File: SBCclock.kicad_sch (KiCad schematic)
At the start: 18 parts, among them J1 clocks, J2 quadrature, J3 power, U1 74HCT14, U2 74HCT163, U3 74HCT112, U4 74ACT07, U5 74HCT153, Y2 GTXO-S14V

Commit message: revised board - tested
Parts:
- added D3: RED, LED_SMD:LED_0805_2012Metric_Pad1.15x1.40mm_HandSolder, symbol Device:LED
- added D4: YELLOW, LED_SMD:LED_0805_2012Metric_Pad1.15x1.40mm_HandSolder, symbol Device:LED
- added D5: GREEN, LED_SMD:LED_0805_2012Metric_Pad1.15x1.40mm_HandSolder, symbol Device:LED
- added R2, R8, R9: 330R, Resistor_SMD:R_0805_2012Metric_Pad1.20x1.40mm_HandSolder, symbol Device:R
- added SW1: SW_Push, Button_Switch_SMD:SW_SPST_B3S-1000, symbol Switch:SW_Push
- added U6: DS1813, Package_TO_SOT_SMD:SOT-23-3, symbol 6309sbc:DS1813
- added U7: 74AHC1G14, Package_TO_SOT_SMD:SOT-353_SC-70-5_Handsoldering, symbol 74xGxx:74AHC1G14
- J1: footprint Connector_PinHeader_2.54mm:PinHeader_1x07_P2.54mm_Vertical -> Connector_PinHeader_2.54mm:PinHeader_1x08_P2.54mm_Vertical; symbol Connector_Generic:Conn_01x07 -> Connector_Generic:Conn_01x08
- J2: footprint Connector_PinHeader_2.54mm:PinHeader_1x06_P2.54mm_Vertical -> Connector_PinHeader_2.54mm:PinHeader_1x04_P2.54mm_Vertical; symbol Connector_Generic:Conn_01x06 -> Connector_Generic:Conn_01x04
- U4: DigiKey (none) -> 296-SN74ACT07PWRCT-ND
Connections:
- net +5V: now also D5.2 (A), U6.2 (VCC), U7.5 (VCC)
- net E: now also J2.1 (Pin_1); no longer J2.2 (Pin_2)
- net GND: now also R2.2, R8.2, R9.2, SW1.2, U6.3 (GND), U7.3 (GND); no longer J2.1 (Pin_1)
- net Q: now also J2.3 (Pin_3); no longer J2.5 (Pin_5)
- net ~{E}: now also J2.2 (Pin_2); no longer J2.3 (Pin_3)
- net ~{Q}: now also J2.4 (Pin_4); no longer J2.6 (Pin_6)
- net ~{RESET}: now also D4.2 (A), SW1.1, U6.1 (~{RST}), U7.2
- new net: D3.2 (A), U7.4
- new net: D5.1 (K), R9.1
- new net: D4.1 (K), R8.1
- new net: D3.1 (K), R2.1
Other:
- moved on the sheet: C5, R3, U2

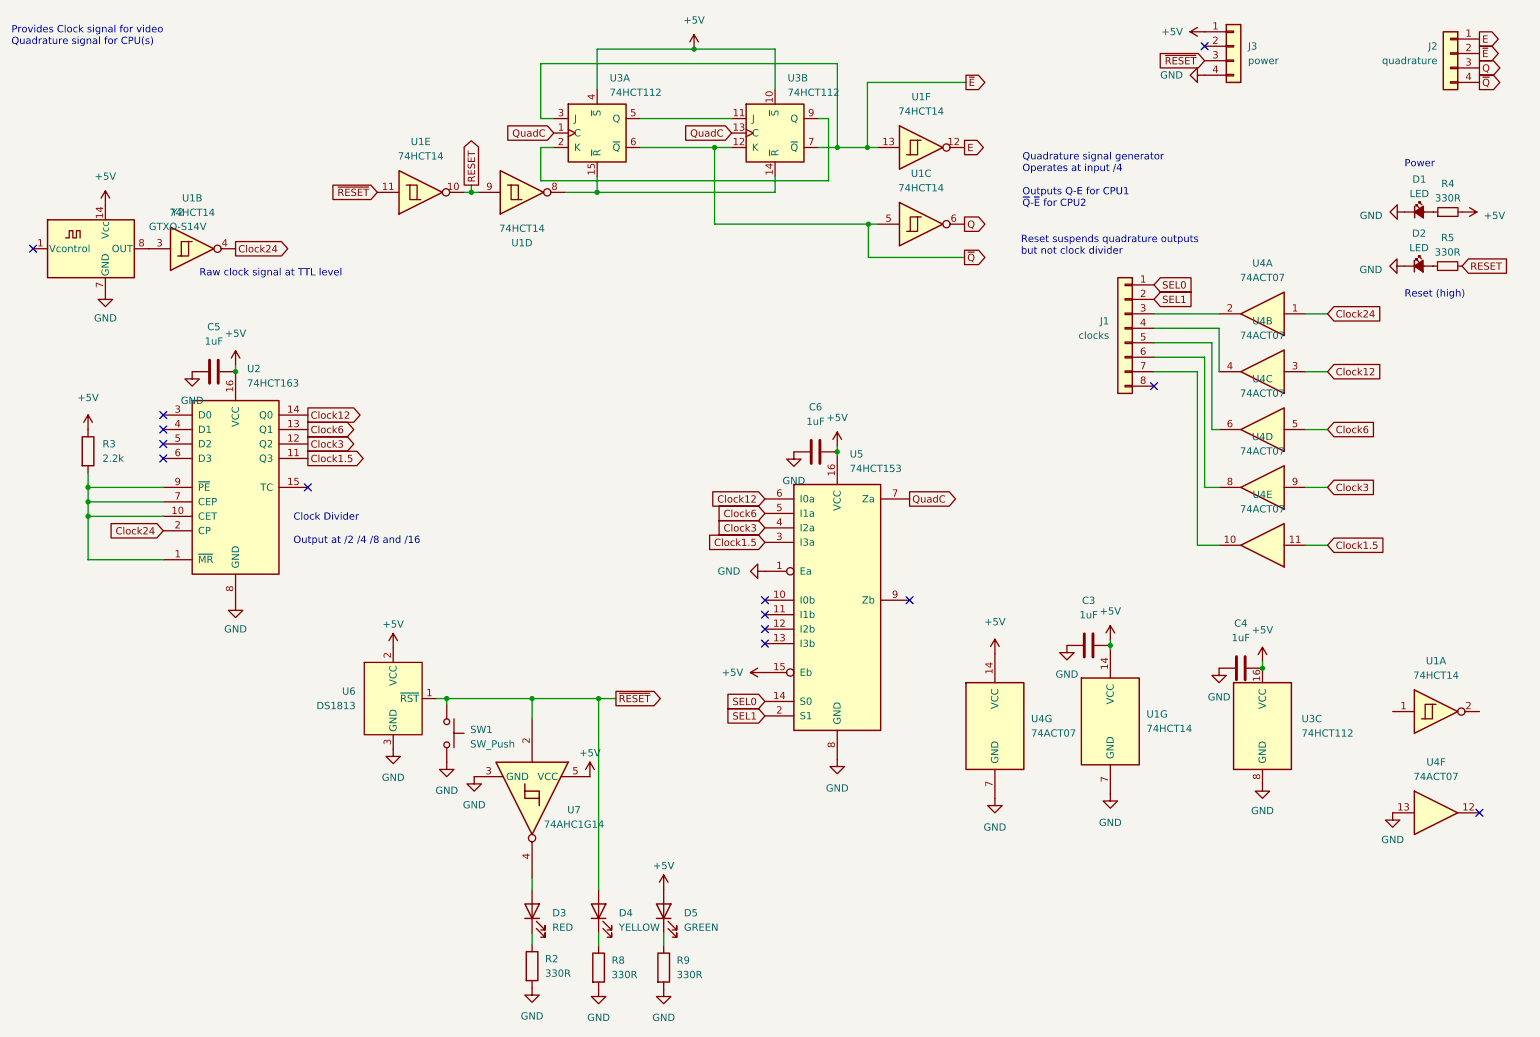
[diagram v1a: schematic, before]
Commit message: remove redundant single gate
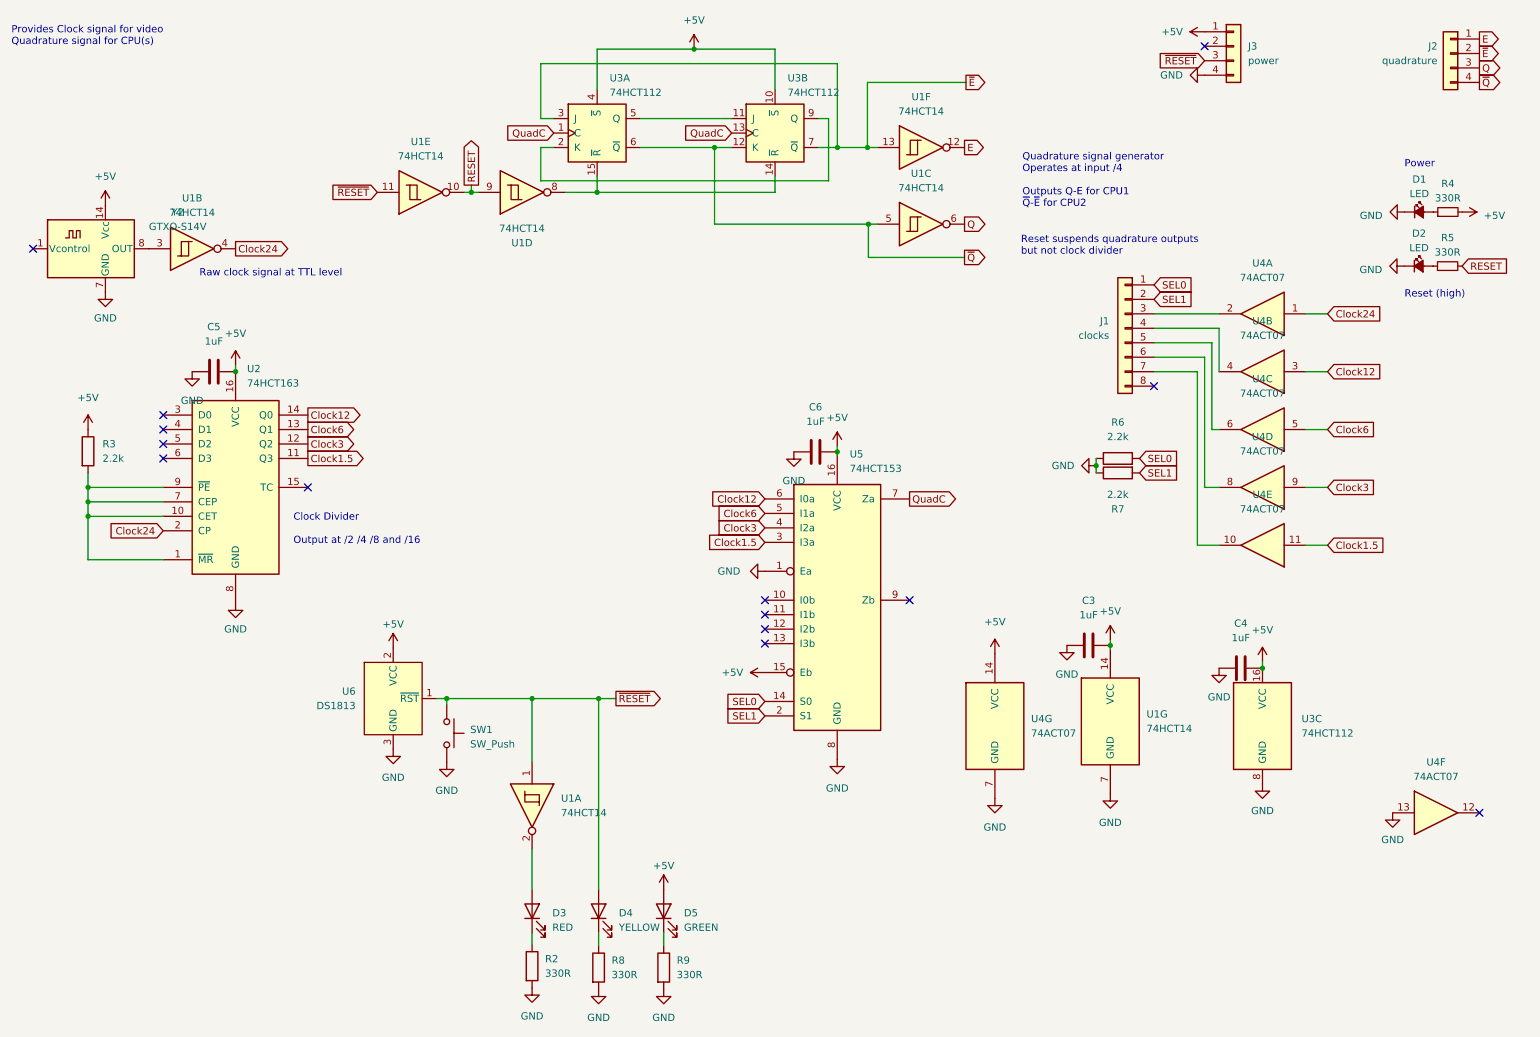
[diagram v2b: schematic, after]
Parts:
- removed U7: 74AHC1G14, Package_TO_SOT_SMD:SOT-353_SC-70-5_Handsoldering, symbol 74xGxx:74AHC1G14
- added R6, R7: 2.2k, Resistor_SMD:R_0805_2012Metric_Pad1.20x1.40mm_HandSolder, symbol Device:R
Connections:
- net GND: now also R6.1, R7.1
- net SEL0: now also R6.2
- net SEL1: now also R7.2
- net ~{RESET}: now also U1.1
- net at D3.2 (A): now also U1.2
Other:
- moved on the sheet: U1A

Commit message: update
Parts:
- removed D1, D2: LED, LED_SMD:LED_0805_2012Metric_Pad1.15x1.40mm_HandSolder, symbol Device:LED_Small_Filled
- removed R4, R5: 330R, Resistor_SMD:R_0805_2012Metric_Pad1.20x1.40mm_HandSolder, symbol Device:R_Small
- SW1: value SW_Push -> RESET
- Y2: footprint Oscillator:Oscillator_DIP-14 -> Library:Oscillator_DIP-8+14
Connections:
- net GND: now also U1.1
- net RESET: now also D3.2 (A)
- net ~{RESET}: no longer U1.1
- net at U1.2: no longer D3.2 (A)
- net Clock1.5 renamed Clock/16
- net Clock12 renamed Clock/2
- net Clock24 renamed ClockBase
- net Clock3 renamed Clock/8
- net Clock6 renamed Clock/4
- no-connect marks 14 -> 15
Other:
- note removed: "Power"
- note removed: "Reset (high)"
- title: (none) -> SBC Clock Generator
- moved on the sheet: U1A, U4F

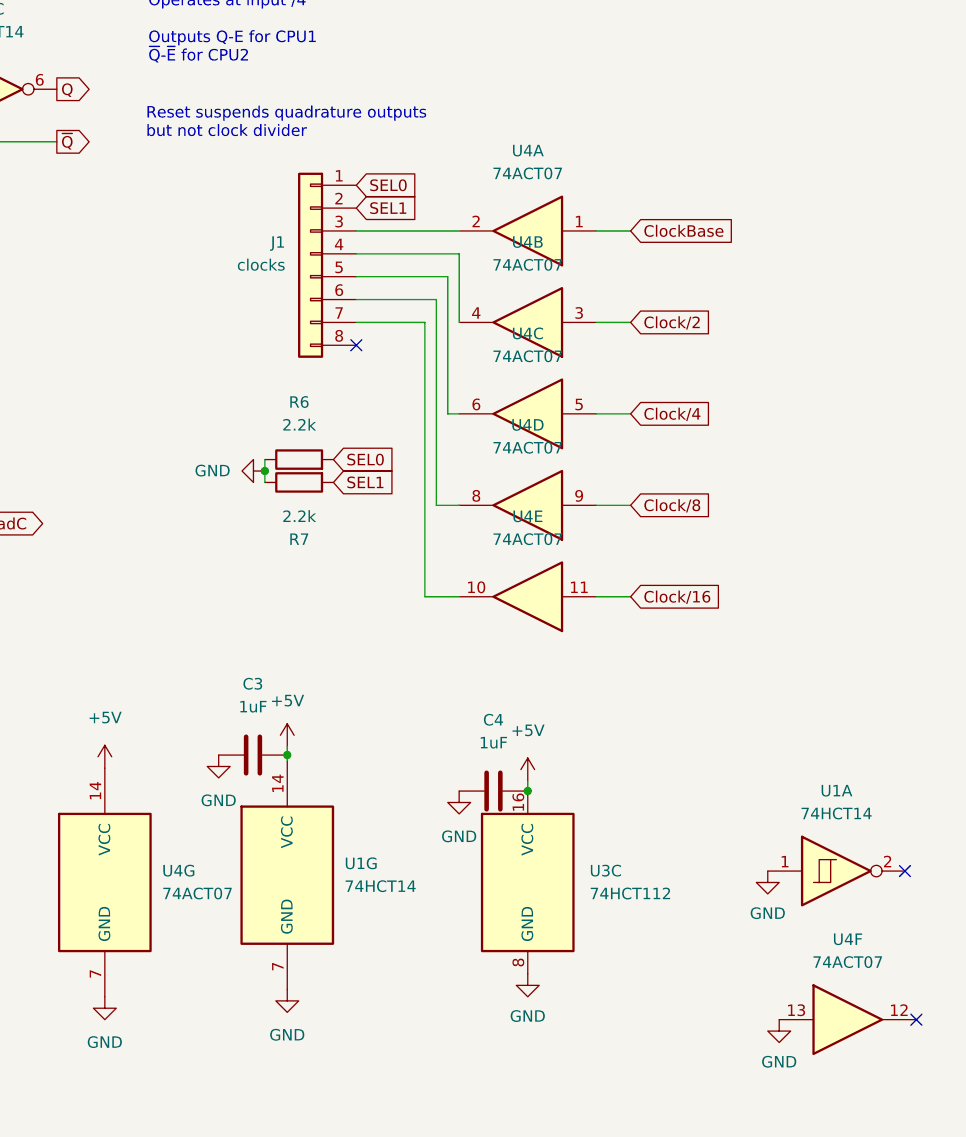
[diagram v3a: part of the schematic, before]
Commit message: fix u4 footprint
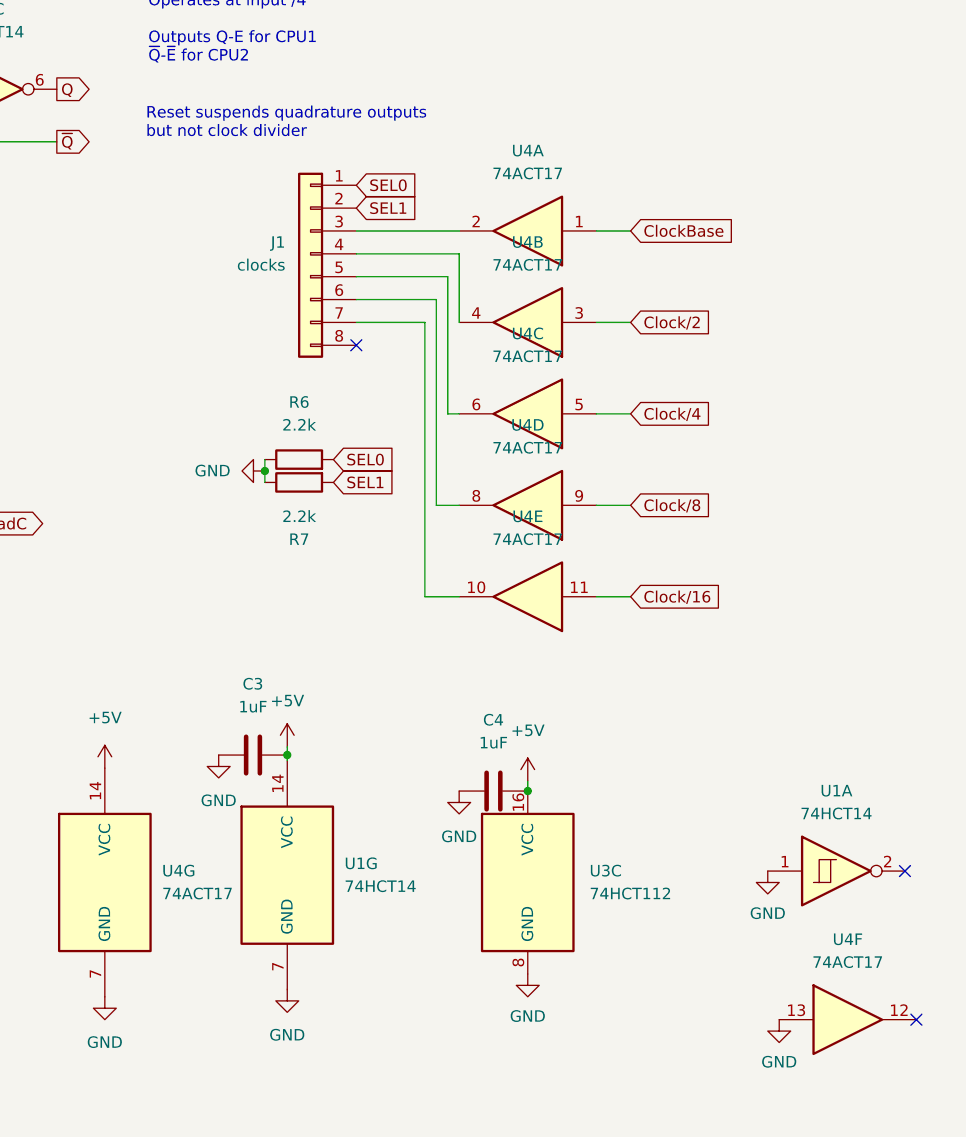
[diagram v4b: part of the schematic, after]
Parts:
- U4: value 74ACT07 -> 74ACT17; footprint Package_SO:TSSOP-14_4.4x3.6mm_P0.4mm -> Package_SO:TSSOP-14_4.4x5mm_P0.65mm; DigiKey 296-SN74ACT07PWRCT-ND -> 296-SN74ACT17PWRCT-ND
- U6: DigiKey (none) -> DS1813R-5+CT-ND
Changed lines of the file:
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@@
 			)
 		)
-		(property "Value" "74ACT07"
+		(property "Value" "74ACT17"
 			(at 234.95 62.23 0)
 			(effects
@@
 			)
 		)
-		(property "Footprint" "Package_SO:TSSOP-14_4.4x3.6mm_P0.4mm"
+		(property "Footprint" "Package_SO:TSSOP-14_4.4x5mm_P0.65mm"
 			(at 234.95 68.58 0)
 			(effects
@@
 			)
 		)
-		(property "DigiKey" "296-SN74ACT07PWRCT-ND"
+		(property "DigiKey" "296-SN74ACT17PWRCT-ND"
 			(at 234.95 68.58 0)
 			(effects
@@
 			)
 		)
-		(property "Value" "74ACT07"
+		(property "Value" "74ACT17"
 			(at 234.95 92.71 0)
 			(effects
@@
 			)
 		)
-		(property "Footprint" "Package_SO:TSSOP-14_4.4x3.6mm_P0.4mm"
+		(property "Footprint" "Package_SO:TSSOP-14_4.4x5mm_P0.65mm"
 			(at 234.95 99.06 0)
 			(effects
@@
 			)
 		)
-		(property "DigiKey" "296-SN74ACT07PWRCT-ND"
+		(property "DigiKey" "296-SN74ACT17PWRCT-ND"
 			(at 234.95 99.06 0)
 			(effects
@@
 			)
 		)
-		(property "Value" "74ACT07"
+		(property "Value" "74ACT17"
 			(at 234.95 72.39 0)
 			(effects
@@
 			)
 		)
-		(property "Footprint" "Package_SO:TSSOP-14_4.4x3.6mm_P0.4mm"
+		(property "Footprint" "Package_SO:TSSOP-14_4.4x5mm_P0.65mm"
 			(at 234.95 78.74 0)
 			(effects
@@
 			)
 		)
-		(property "DigiKey" "296-SN74ACT07PWRCT-ND"
+		(property "DigiKey" "296-SN74ACT17PWRCT-ND"
 			(at 234.95 78.74 0)
 			(effects
@@
 			)
 		)
+		(property "DigiKey" "DS1813R-5+CT-ND"
+			(at 82.296 136.144 0)
+			(effects
+				(font
+					(size 1.27 1.27)
+				)
+				(hide yes)
+			)
+		)
 		(pin "2"
 		)
@@
 			)
 		)
-		(property "Value" "74ACT07"
+		(property "Value" "74ACT17"
 			(at 194.31 142.2399 0)
 			(effects
@@
 			)
 		)
-		(property "Footprint" "Package_SO:TSSOP-14_4.4x3.6mm_P0.4mm"
+		(property "Footprint" "Package_SO:TSSOP-14_4.4x5mm_P0.65mm"
 			(at 187.96 140.97 0)
 			(effects
@@
 			)
 		)
-		(property "DigiKey" "296-SN74ACT07PWRCT-ND"
+		(property "DigiKey" "296-SN74ACT17PWRCT-ND"
 			(at 187.96 140.97 0)
 			(effects
@@
 			)
 		)
-		(property "Value" "74ACT07"
+		(property "Value" "74ACT17"
 			(at 234.95 82.55 0)
 			(effects
@@
 			)
 		)
-		(property "Footprint" "Package_SO:TSSOP-14_4.4x3.6mm_P0.4mm"
+		(property "Footprint" "Package_SO:TSSOP-14_4.4x5mm_P0.65mm"
 			(at 234.95 88.9 0)
 			(effects
@@
 			)
 		)
-		(property "DigiKey" "296-SN74ACT07PWRCT-ND"
+		(property "DigiKey" "296-SN74ACT17PWRCT-ND"
 			(at 234.95 88.9 0)
 			(effects
@@
 			)
 		)
-		(property "Value" "74ACT07"
+		(property "Value" "74ACT17"
 			(at 270.51 149.86 0)
 			(effects
@@
 			)
 		)
-		(property "Footprint" "Package_SO:TSSOP-14_4.4x3.6mm_P0.4mm"
+		(property "Footprint" "Package_SO:TSSOP-14_4.4x5mm_P0.65mm"
 			(at 270.51 156.21 0)
 			(effects
@@
 			)
 		)
-		(property "DigiKey" "296-SN74ACT07PWRCT-ND"
+		(property "DigiKey" "296-SN74ACT17PWRCT-ND"
 			(at 270.51 156.21 0)
 			(effects
@@
 			)
 		)
-		(property "Value" "74ACT07"
+		(property "Value" "74ACT17"
 			(at 234.95 102.87 0)
 			(effects
@@
 			)
 		)
-		(property "Footprint" "Package_SO:TSSOP-14_4.4x3.6mm_P0.4mm"
+		(property "Footprint" "Package_SO:TSSOP-14_4.4x5mm_P0.65mm"
 			(at 234.95 109.22 0)
 			(effects
@@
 			)
 		)
-		(property "DigiKey" "296-SN74ACT07PWRCT-ND"
+		(property "DigiKey" "296-SN74ACT17PWRCT-ND"
 			(at 234.95 109.22 0)
 			(effects
